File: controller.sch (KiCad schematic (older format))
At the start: 18 parts, among them J1 Conn_01x16_Female, J2 Conn_01x08_Female, SW1 SW_Push, U1 ATmega32U4-AU, Y1 16MHz

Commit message: footprints assigned
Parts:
- J1: footprint (none) -> Connector_PinSocket_2.54mm:PinSocket_1x16_P2.54mm_Vertical
- J2: footprint (none) -> Connector_PinSocket_2.54mm:PinSocket_1x08_P2.54mm_Vertical
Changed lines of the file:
@@
 EESchema Schematic File Version 4
+LIBS:controller-cache
 EELAYER 30 0
 EELAYER END
@@
 F 0 "J1" H 5878 2126 50  0000 L CNN
 F 1 "Conn_01x16_Female" H 5878 2035 50  0000 L CNN
-F 2 "" H 5850 2150 50  0001 C CNN
+F 2 "Connector_PinSocket_2.54mm:PinSocket_1x16_P2.54mm_Vertical" H 5850 2150 50  0001 C CNN
 F 3 "~" H 5850 2150 50  0001 C CNN
 	1    5850 2150
@@
 F 0 "J2" H 5878 3476 50  0000 L CNN
 F 1 "Conn_01x08_Female" H 5878 3385 50  0000 L CNN
-F 2 "" H 5850 3500 50  0001 C CNN
+F 2 "Connector_PinSocket_2.54mm:PinSocket_1x08_P2.54mm_Vertical" H 5850 3500 50  0001 C CNN
 F 3 "~" H 5850 3500 50  0001 C CNN
 	1    5850 3500

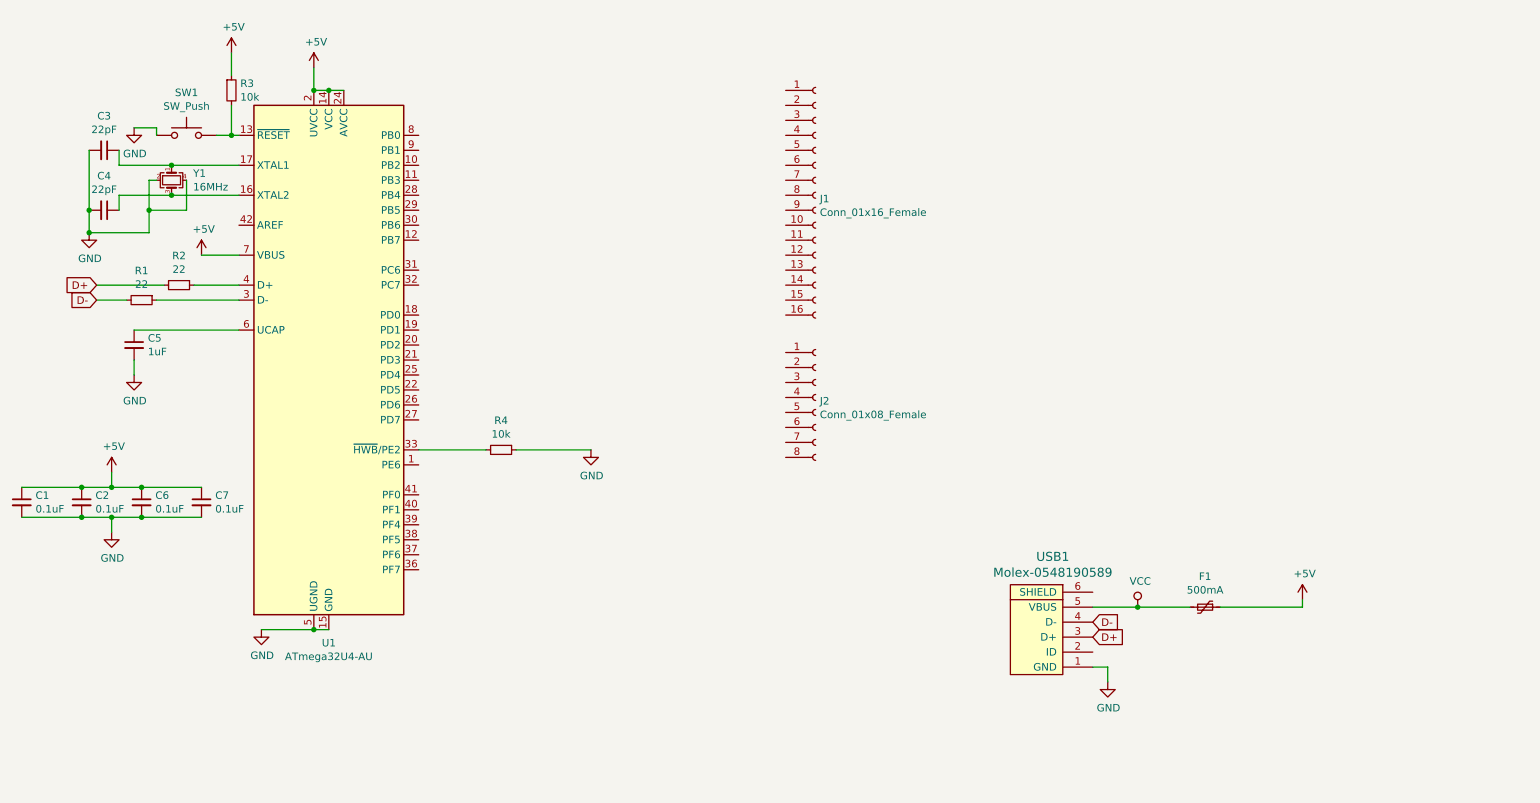
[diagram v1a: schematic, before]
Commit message: changed to at90usb1286 and cleanup
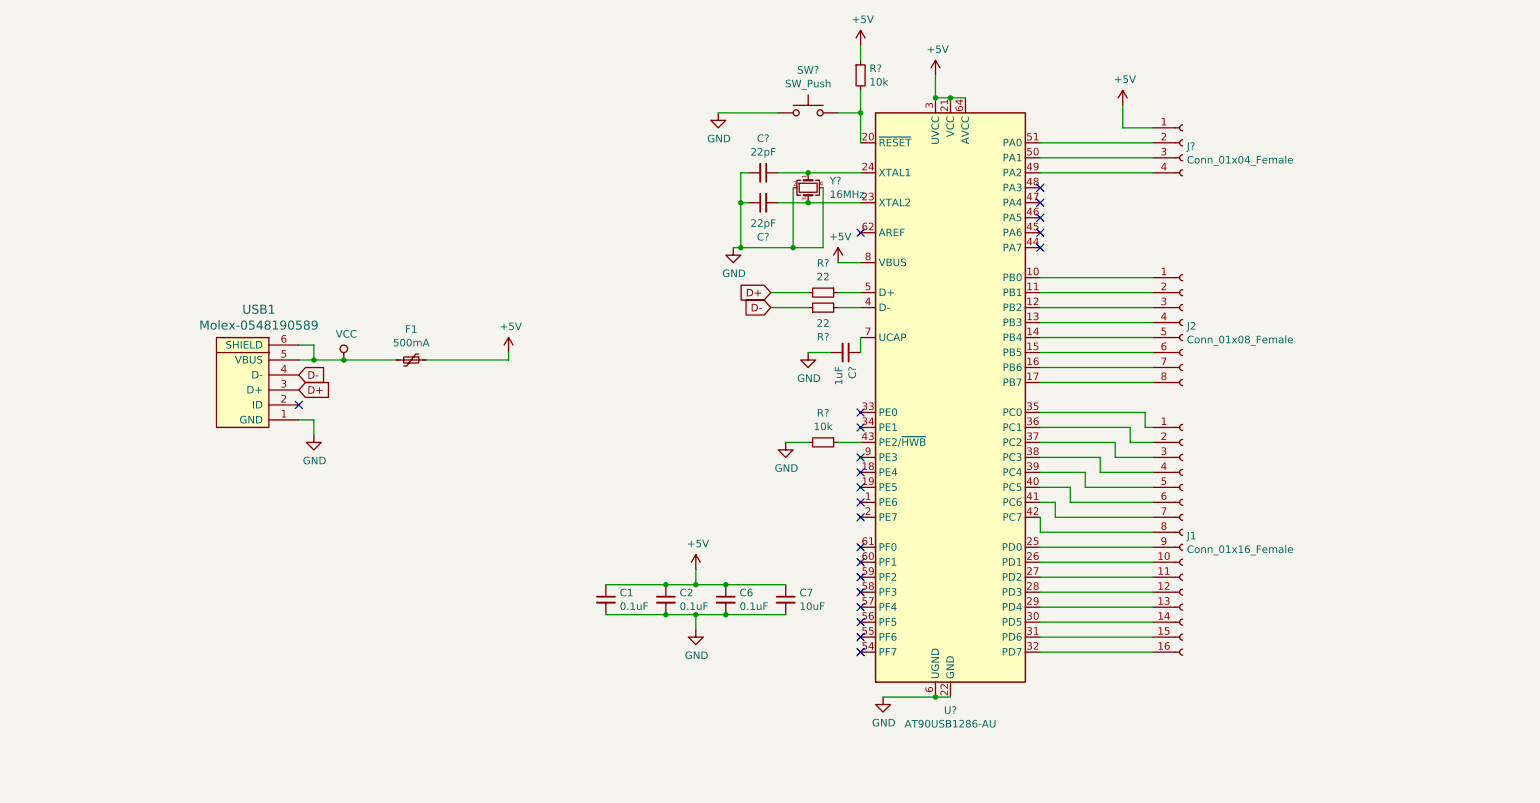
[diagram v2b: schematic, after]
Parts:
- removed C3, C4: 22pF, Capacitor_SMD:C_0805_2012Metric, symbol Device:C_Small
- removed C5: 1uF, Capacitor_SMD:C_0805_2012Metric, symbol Device:C_Small
- removed R1, R2: 22, Resistor_SMD:R_0805_2012Metric, symbol Device:R_Small
- removed R3, R4: 10k, Resistor_SMD:R_0805_2012Metric, symbol Device:R_Small
- removed SW1: SW_Push, random-keyboard-parts:SKQG-1155865, symbol Switch:SW_Push
- removed U1: ATmega32U4-AU, Package_QFP:TQFP-44_10x10mm_P0.8mm, symbol MCU_Microchip_ATmega:ATmega32U4-AU
- removed Y1: 16MHz, Crystal:Crystal_SMD_3225-4Pin_3.2x2.5mm, symbol Device:Crystal_GND24_Small
- added C?: 1uF, Capacitor_SMD:C_0805_2012Metric, symbol Device:C_Small
- added C? (x2): 22pF, Capacitor_SMD:C_0805_2012Metric, symbol Device:C_Small
- added J?: Conn_01x04_Female, symbol Connector:Conn_01x04_Female
- added R? (x2): 10k, Resistor_SMD:R_0805_2012Metric, symbol Device:R_Small
- added R? (x2): 22, Resistor_SMD:R_0805_2012Metric, symbol Device:R_Small
- added SW?: SW_Push, random-keyboard-parts:SKQG-1155865, symbol Switch:SW_Push
- added U?: AT90USB1286-AU, Package_QFP:TQFP-64_14x14mm_P0.8mm, symbol MCU_Microchip_AVR:AT90USB1286-AU
- added Y?: 16MHz, Crystal:Crystal_SMD_3225-4Pin_3.2x2.5mm, symbol Device:Crystal_GND24_Small
- C7: value 0.1uF -> 10uF
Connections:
- net +5V: now also J?.1 (Pin_1), R?.1, U?.21 (VCC), U?.3 (UVCC), U?.52 (VCC), U?.64 (AVCC), U?.8 (VBUS)
- net D+: now also R?.2
- net D-: now also R?.1
- net GND: now also C?.1, C?.2, C?.2, R?.2, SW?.1, U?.22 (GND), U?.53 (GND), U?.6 (UGND), U?.63 (GND), Y?.2, Y?.4
- net VCC: now also USB1.6 (SHIELD)
- net at J1.1 (Pin_1): now also U?.35 (PC0)
- net at J1.10 (Pin_10): now also U?.26 (PD1)
- net at J1.11 (Pin_11): now also U?.27 (PD2)
- net at J1.12 (Pin_12): now also U?.28 (PD3)
- net at J1.13 (Pin_13): now also U?.29 (PD4)
- net at J1.14 (Pin_14): now also U?.30 (PD5)
- net at J1.15 (Pin_15): now also U?.31 (PD6)
- net at J1.16 (Pin_16): now also U?.32 (PD7)
- net at J1.2 (Pin_2): now also U?.36 (PC1)
- net at J1.3 (Pin_3): now also U?.37 (PC2)
- net at J1.4 (Pin_4): now also U?.38 (PC3)
- net at J1.5 (Pin_5): now also U?.39 (PC4)
- net at J1.6 (Pin_6): now also U?.40 (PC5)
- net at J1.7 (Pin_7): now also U?.41 (PC6)
- net at J1.8 (Pin_8): now also U?.42 (PC7)
- net at J1.9 (Pin_9): now also U?.25 (PD0)
- net at J2.1 (Pin_1): now also U?.10 (PB0)
- net at J2.2 (Pin_2): now also U?.11 (PB1)
- net at J2.3 (Pin_3): now also U?.12 (PB2)
- net at J2.4 (Pin_4): now also U?.13 (PB3)
- net at J2.5 (Pin_5): now also U?.14 (PB4)
- net at J2.6 (Pin_6): now also U?.15 (PB5)
- net at J2.7 (Pin_7): now also U?.16 (PB6)
- net at J2.8 (Pin_8): now also U?.17 (PB7)
- new net: R?.2, SW?.2, U?.20 (~RESET)
- new net: C?.2, U?.23 (XTAL2), Y?.3
- new net: C?.1, U?.24 (XTAL1), Y?.1
- new net: R?.2, U?.4 (D-)
- new net: R?.1, U?.43 (PE2/~HWB)
- new net: J?.4 (Pin_4), U?.49 (PA2)
- new net: R?.1, U?.5 (D+)
- new net: J?.3 (Pin_3), U?.50 (PA1)
- new net: J?.2 (Pin_2), U?.51 (PA0)
- new net: C?.1, U?.7 (UCAP)
- no-connect marks 0 -> 22
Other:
- moved on the sheet: C1, C2, C6, C7, F1, J1, J2, USB1

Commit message: pcb design
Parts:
- removed J1: Conn_01x16_Female, Connector_PinSocket_2.54mm:PinSocket_1x16_P2.54mm_Vertical, symbol Connector:Conn_01x16_Female
- removed J2: Conn_01x08_Female, Connector_PinSocket_2.54mm:PinSocket_1x08_P2.54mm_Vertical, symbol Connector:Conn_01x08_Female
- removed J?: Conn_01x04_Female, symbol Connector:Conn_01x04_Female
- removed USB1: Molex-0548190589, random-keyboard-parts:Molex-0548190589, symbol random-keyboard-parts:Molex-0548190589
- added J1: Conn_01x04, Connector_PinHeader_2.54mm:PinHeader_1x04_P2.54mm_Vertical, symbol Connector_Generic:Conn_01x04
- added J2: Conn_01x08, Connector_PinHeader_2.54mm:PinHeader_1x08_P2.54mm_Vertical, symbol Connector_Generic:Conn_01x08
- added J3: Conn_01x16, Connector_PinHeader_2.54mm:PinHeader_1x16_P2.54mm_Vertical, symbol Connector_Generic:Conn_01x16
- added R1, R2: 5.1k, Resistor_SMD:R_0805_2012Metric, symbol Device:R_Small
- added R7, R8, R9: 470, Resistor_SMD:R_0805_2012Metric, symbol Device:R_Small
- added U1: PRTR5V0U2X, random-keyboard-parts:SOT143B, symbol random-keyboard-parts:PRTR5V0U2X
- added USB1: HRO-TYPE-C-31-M-12, Type-C:HRO-TYPE-C-31-M-12-HandSoldering, symbol Type-C:HRO-TYPE-C-31-M-12
- gave numbers to parts that had none: 10
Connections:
- net +5V: now also J1.2 (Pin_2), U1.4 (VCC)
- net D+: now also U1.2 (IO1), USB1.6 (DP1), USB1.8 (DP2)
- net D-: now also U1.3 (IO2), USB1.5 (DN2), USB1.7 (DN1)
- net GND: now also USB1.1 (GND), USB1.12 (GND), USB1.13 (SHIELD)
- net VCC: now also USB1.11 (VBUS), USB1.2 (VBUS)
- net at U2.35 (PC0): now also J2.1 (Pin_1)
- net at U2.30 (PD5): now also R7.2
- net at U2.31 (PD6): now also R8.2
- net at U2.32 (PD7): now also R9.1
- net at U2.36 (PC1): now also J2.2 (Pin_2)
- net at U2.37 (PC2): now also J2.3 (Pin_3)
- net at U2.38 (PC3): now also J2.4 (Pin_4)
- net at U2.39 (PC4): now also J2.5 (Pin_5)
- net at U2.40 (PC5): now also J2.6 (Pin_6)
- net at U2.41 (PC6): now also J2.7 (Pin_7)
- net at U2.42 (PC7): now also J2.8 (Pin_8)
- net at U2.1 (PE6): now also J3.16 (Pin_16)
- net at U2.2 (PE7): now also J3.15 (Pin_15)
- net 1: now reaches U2.46 (PA5)
- net 1: now also J3.1 (Pin_1)
- net 2: now reaches U2.47 (PA4)
- net 2: now also J3.2 (Pin_2)
- net 3: now reaches U2.48 (PA3)
- net 3: now also J3.3 (Pin_3)
- net 4: now reaches U2.49 (PA2)
- net 4: now also J3.4 (Pin_4)
- net 5: now reaches U2.50 (PA1)
- net 5: now also J3.5 (Pin_5)
- net 6: now reaches U2.51 (PA0)
- net 6: now also J3.6 (Pin_6)
- net at U2.54 (PF7): now also J3.7 (Pin_7)
- net at U2.55 (PF6): now also J3.8 (Pin_8)
- net at U2.56 (PF5): now also J3.9 (Pin_9)
- net at U2.57 (PF4): now also J3.10 (Pin_10)
- net at U2.58 (PF3): now also J3.11 (Pin_11)
- net at U2.59 (PF2): now also J3.12 (Pin_12)
- net at U2.60 (PF1): now also J3.13 (Pin_13)
- net at U2.61 (PF0): now also J3.14 (Pin_14)
- new net: R2.1, USB1.10 (CC2)
- new net: R1.1, USB1.4 (CC1)
- new net: R1.2, R2.2, U1.1 (GND)
- new net: J1.1 (Pin_1), R7.1
- new net: J1.3 (Pin_3), R8.1
- new net: J1.4 (Pin_4), R9.2
- no-connect marks 22 -> 8
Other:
- moved on the sheet: C1, C2, C6, C7

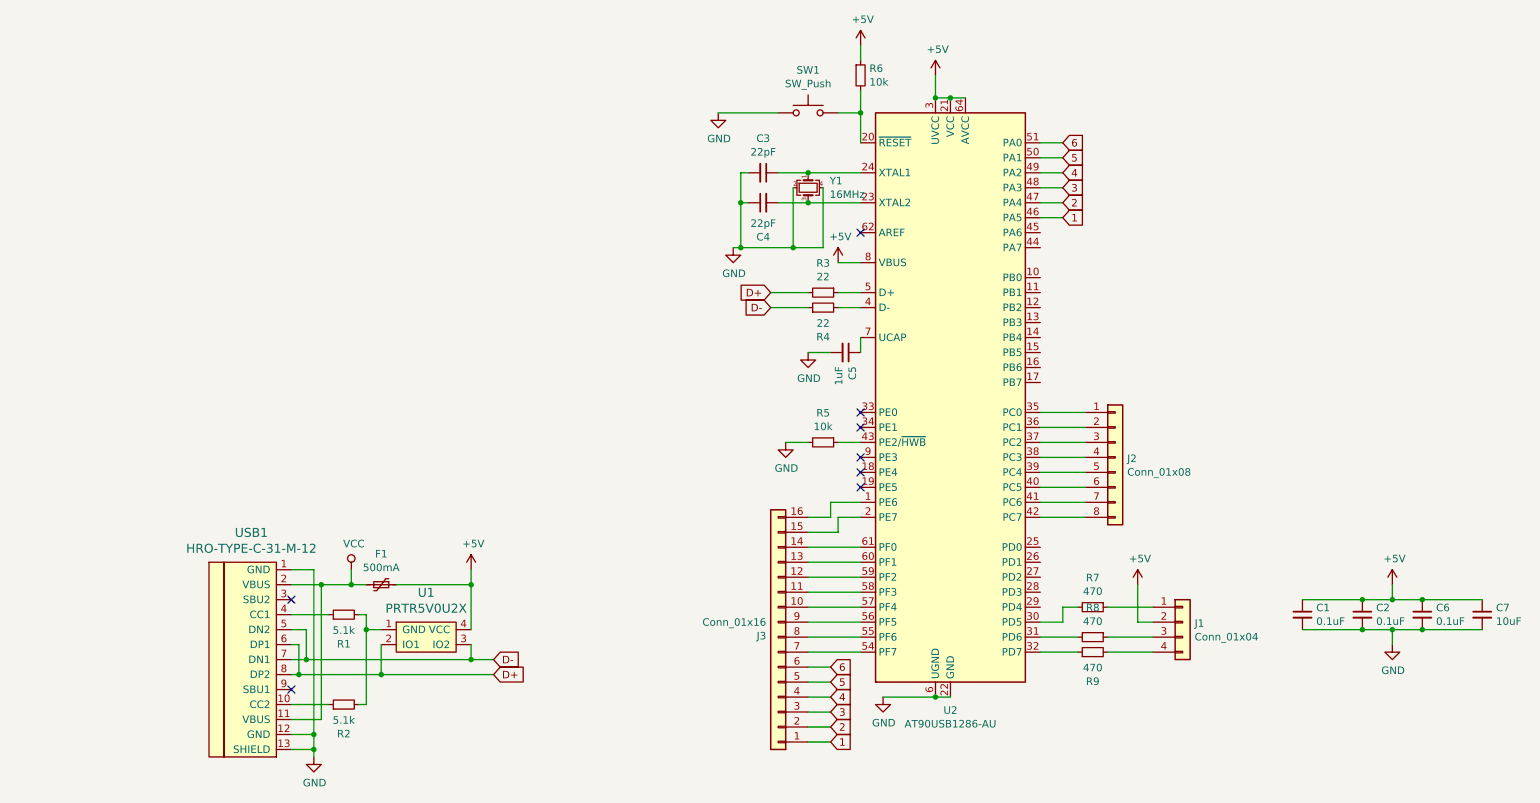
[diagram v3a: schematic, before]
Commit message: misc tweaks for shield and usb pathing
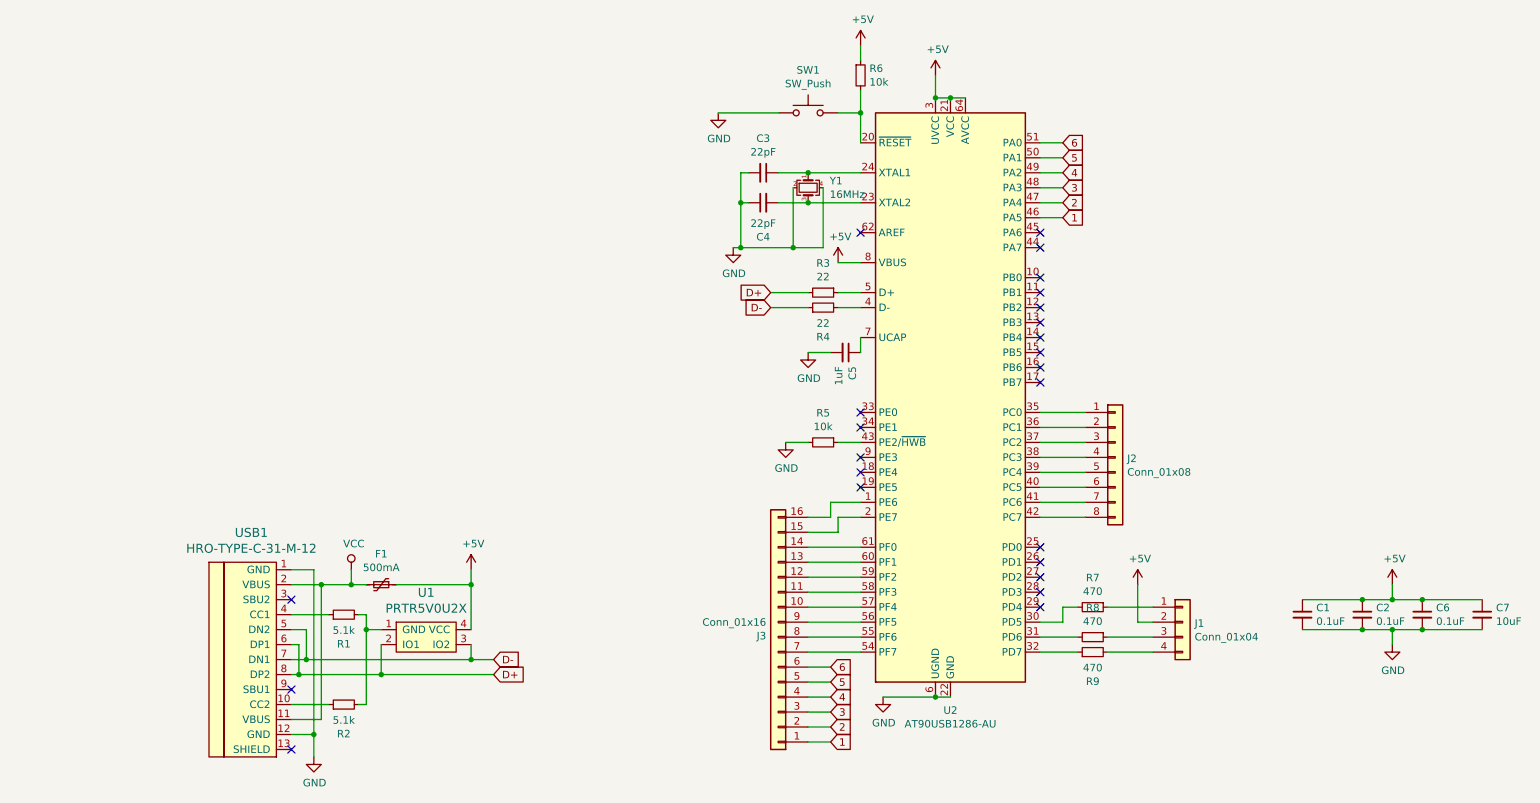
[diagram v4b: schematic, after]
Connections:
- net GND: no longer USB1.13 (SHIELD)
- no-connect marks 8 -> 24
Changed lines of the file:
@@
 	2500 4650 2500 5750
-Wire Wire Line
-	2500 5850 2350 5850
 Wire Wire Line
 	2350 5750 2500 5750
 Connection ~ 2500 5750
-Wire Wire Line
-	2500 5750 2500 5850
 $Comp
 L power:GND #PWR0112
@@
 	1    0    0    -1
 $EndComp
-Wire Wire Line
-	2500 5900 2500 5850
-Connection ~ 2500 5850
 Wire Wire Line
 	2350 5350 2400 5350
@@
 Wire Wire Line
 	7350 1800 7500 1800
+Wire Wire Line
+	2500 5750 2500 5900
+NoConn ~ 2350 5850
+NoConn ~ 7350 4900
+NoConn ~ 7350 4800
+NoConn ~ 7350 4700
+NoConn ~ 7350 4600
+NoConn ~ 7350 4500
+NoConn ~ 7350 3400
+NoConn ~ 7350 3300
+NoConn ~ 7350 3200
+NoConn ~ 7350 3100
+NoConn ~ 7350 3000
+NoConn ~ 7350 2900
+NoConn ~ 7350 2800
+NoConn ~ 7350 2700
+NoConn ~ 7350 2500
+NoConn ~ 7350 2400
 $EndSCHEMATC

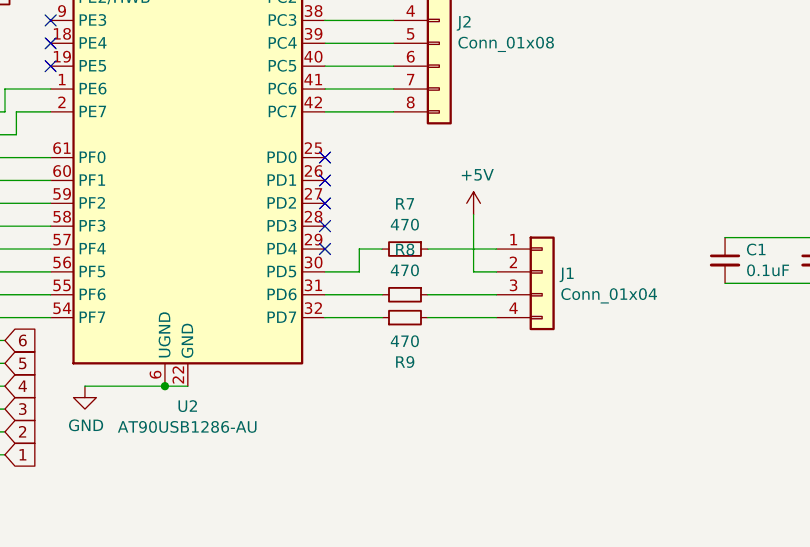
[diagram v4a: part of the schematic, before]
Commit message: clarified resistor value
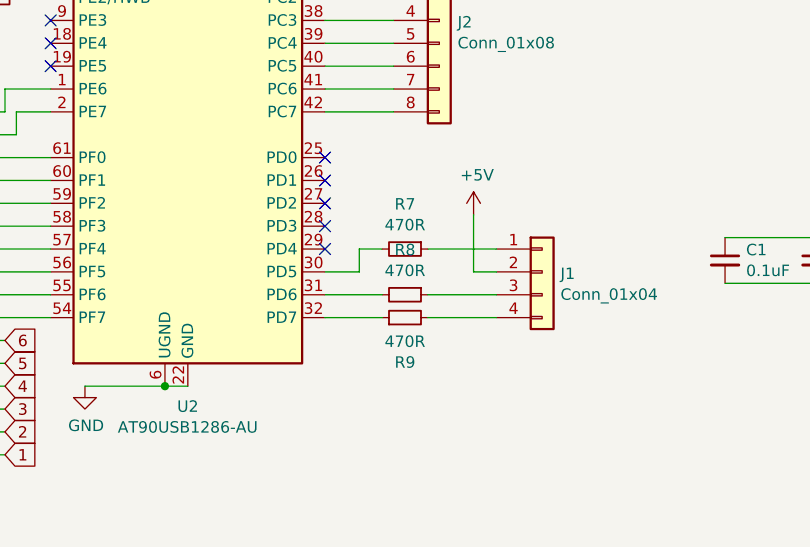
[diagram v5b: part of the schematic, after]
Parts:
- R7, R8, R9: value 470 -> 470R
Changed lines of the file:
@@
 P 7700 4900
 F 0 "R7" V 7504 4900 50  0000 C CNN
-F 1 "470" V 7595 4900 50  0000 C CNN
+F 1 "470R" V 7595 4900 50  0000 C CNN
 F 2 "Resistor_SMD:R_0805_2012Metric" H 7700 4900 50  0001 C CNN
 F 3 "~" H 7700 4900 50  0001 C CNN
 	1    7700 4900
-	0    1    1    0
-$EndComp
-$Comp
-L Device:R_Small R8
-U 1 1 5DD1D4DA
-P 7700 5100
-F 0 "R8" V 7504 5100 50  0000 C CNN
-F 1 "470" V 7595 5100 50  0000 C CNN
-F 2 "Resistor_SMD:R_0805_2012Metric" H 7700 5100 50  0001 C CNN
-F 3 "~" H 7700 5100 50  0001 C CNN
-	1    7700 5100
 	0    1    1    0
 $EndComp
@@
 P 7700 5200
 F 0 "R9" V 7504 5200 50  0000 C CNN
-F 1 "470" V 7595 5200 50  0000 C CNN
+F 1 "470R" V 7595 5200 50  0000 C CNN
 F 2 "Resistor_SMD:R_0805_2012Metric" H 7700 5200 50  0001 C CNN
 F 3 "~" H 7700 5200 50  0001 C CNN
@@
 NoConn ~ 7350 2500
 NoConn ~ 7350 2400
+$Comp
+L Device:R_Small R8
+U 1 1 5DD1D4DA
+P 7700 5100
+F 0 "R8" V 7504 5100 50  0000 C CNN
+F 1 "470R" V 7595 5100 50  0000 C CNN
+F 2 "Resistor_SMD:R_0805_2012Metric" H 7700 5100 50  0001 C CNN
+F 3 "~" H 7700 5100 50  0001 C CNN
+	1    7700 5100
+	0    1    1    0
+$EndComp
 $EndSCHEMATC
